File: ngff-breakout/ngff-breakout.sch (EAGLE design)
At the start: 79 parts, among them U1 MIC5366-1.8YC5, U2 MCP1827S-3302E/EB, X1 PINHD-2X4, X10 ZX360D-B-10P(30), X2 692121030100, X3 PINHD-2X10, X4 PINHD-2X5, X5 694108106102, X6 PINHD-1X3, X7 5-1814832-1, X8 5-1814832-1, X9 5-1814832-1, Y1 MHF4, Y2 MHF4, Y3 MHF4

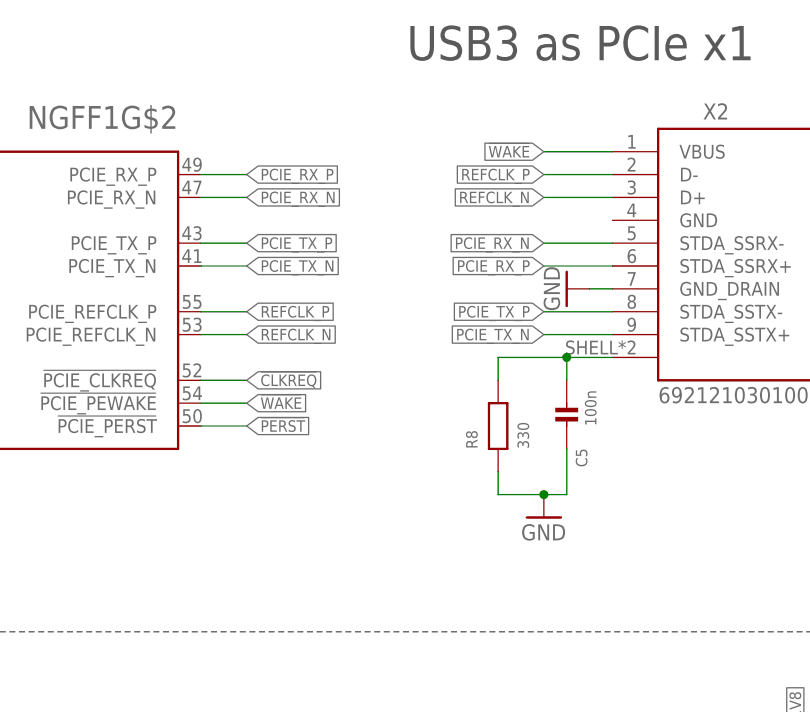
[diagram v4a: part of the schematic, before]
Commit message: ngff: swap Rx and Tx (solves OS#4230)
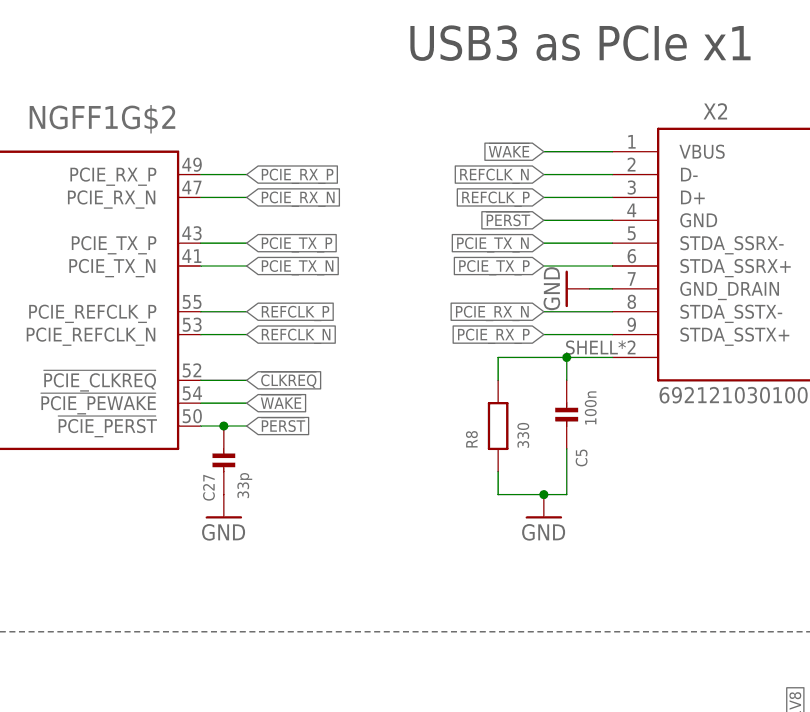
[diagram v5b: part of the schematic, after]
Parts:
- added C27: 33p, rc-sysmocom:CAP_CERAMIC_0402
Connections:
- net !PERST: now also C27.1, X2.GND
- net GND: now also C27.2
- net PCIE_RX_N: now also X2.STDA_SSTX-; no longer X2.STDA_SSRX-
- net PCIE_RX_P: now also X2.STDA_SSTX+; no longer X2.STDA_SSRX+
- net PCIE_TX_N: now also X2.STDA_SSRX-; no longer X2.STDA_SSTX+
- net PCIE_TX_P: now also X2.STDA_SSRX+; no longer X2.STDA_SSTX-
- net REFCLK_N: now also X2.D-; no longer X2.D+
- net REFCLK_P: now also X2.D+; no longer X2.D-
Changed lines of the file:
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@@
 </part>
 <part name="GND29" library="supply1" deviceset="GND" device=""/>
+<part name="C27" library="rc-sysmocom" deviceset="CAP_CERAMIC" device="_0402" value="33p">
+<attribute name="CLASS" value="CAPACITOR"/>
+<attribute name="DESCRIPTION" value="CAP CER 33PF 50V NP0 0402"/>
+<attribute name="LINK" value="http://www.digikey.de/product-detail/de/CL05C330JB5NNNC/1276-1272-1-ND/3889358"/>
+<attribute name="MANUFACTURER" value="Samsung Electro-Mechanics America, Inc."/>
+<attribute name="MANUFACTURERPARTNUMBER" value="CL05C330JB5NNNC"/>
+<attribute name="POPULATED" value="TRUE"/>
+<attribute name="ROHSCERTIFICATE" value="Bleifrei / RoHS-konform"/>
+<attribute name="SOURCE" value="DIGIKEY"/>
+<attribute name="SOURCEPARTNUMBER" value="1276-1272-1-ND"/>
+</part>
+<part name="GND36" library="supply1" deviceset="GND" device=""/>
 </parts>
 <sheets>
@@
 </instance>
 <instance part="GND29" gate="1" x="83.82" y="218.44" rot="R270"/>
+<instance part="C27" gate="G$1" x="45.72" y="200.66" smashed="yes" rot="R270">
+<attribute name="NAME" x="44.704" y="194.818" size="1.27" layer="95" rot="R90"/>
+<attribute name="VALUE" x="48.514" y="195.072" size="1.27" layer="96" rot="R90"/>
+<attribute name="DESCRIPTION" x="45.72" y="200.66" size="1.778" layer="96" display="off"/>
+<attribute name="MANUFACTURER" x="45.72" y="200.66" size="1.778" layer="96" display="off"/>
+<attribute name="MANUFACTURERPARTNUMBER" x="45.72" y="200.66" size="1.778" layer="96" display="off"/>
+<attribute name="SOURCE" x="45.72" y="200.66" size="1.778" layer="96" display="off"/>
+<attribute name="SOURCEPARTNUMBER" x="45.72" y="200.66" size="1.778" layer="96" display="off"/>
+<attribute name="ROHSCERTIFICATE" x="45.72" y="200.66" size="1.778" layer="96" display="off"/>
+<attribute name="POPULATED" x="45.72" y="200.66" size="1.778" layer="96" display="off"/>
+<attribute name="CLASS" x="45.72" y="200.66" size="1.778" layer="96" display="off"/>
+<attribute name="LINK" x="45.72" y="200.66" size="1.778" layer="96" display="off"/>
+</instance>
+<instance part="GND36" gate="1" x="45.72" y="193.04"/>
 </instances>
 <busses>
@@
 <pinref part="GND29" gate="1" pin="GND"/>
 <wire x1="86.36" y1="218.44" x2="88.9" y2="218.44" width="0.1524" layer="91"/>
+</segment>
+<segment>
+<pinref part="C27" gate="G$1" pin="2"/>
+<pinref part="GND36" gate="1" pin="GND"/>
 </segment>
 </net>
@@
 </segment>
 <segment>
+<label x="81.28" y="231.14" size="1.27" layer="95" rot="R180" xref="yes"/>
+<pinref part="X2" gate="G$1" pin="D-"/>
+<wire x1="81.28" y1="231.14" x2="88.9" y2="231.14" width="0.1524" layer="91"/>
+</segment>
+</net>
+<net name="REFCLK_P" class="1">
+<segment>
+<wire x1="43.18" y1="215.9" x2="48.26" y2="215.9" width="0.1524" layer="91"/>
+<label x="48.26" y="215.9" size="1.27" layer="95" rot="MR180" xref="yes"/>
+<pinref part="NGFF1" gate="G$2" pin="PCIE_REFCLK_P"/>
+</segment>
+<segment>
 <wire x1="88.9" y1="228.6" x2="81.28" y2="228.6" width="0.1524" layer="91"/>
 <label x="81.28" y="228.6" size="1.27" layer="95" rot="R180" xref="yes"/>
 <pinref part="X2" gate="G$1" pin="D+"/>
-</segment>
-</net>
-<net name="REFCLK_P" class="1">
-<segment>
-<wire x1="43.18" y1="215.9" x2="48.26" y2="215.9" width="0.1524" layer="91"/>
-<label x="48.26" y="215.9" size="1.27" layer="95" rot="MR180" xref="yes"/>
-<pinref part="NGFF1" gate="G$2" pin="PCIE_REFCLK_P"/>
-</segment>
-<segment>
-<wire x1="88.9" y1="231.14" x2="81.28" y2="231.14" width="0.1524" layer="91"/>
-<label x="81.28" y="231.14" size="1.27" layer="95" rot="R180" xref="yes"/>
-<pinref part="X2" gate="G$1" pin="D-"/>
 </segment>
 </net>
@@
 </segment>
 <segment>
+<label x="81.28" y="213.36" size="1.27" layer="95" rot="R180" xref="yes"/>
+<pinref part="X2" gate="G$1" pin="STDA_SSTX+"/>
+<wire x1="81.28" y1="213.36" x2="88.9" y2="213.36" width="0.1524" layer="91"/>
+</segment>
+</net>
+<net name="PCIE_RX_N" class="1">
+<segment>
+<pinref part="NGFF1" gate="G$2" pin="PCIE_RX_N"/>
+<wire x1="43.18" y1="228.6" x2="48.26" y2="228.6" width="0.1524" layer="91"/>
+<label x="48.26" y="228.6" size="1.27" layer="95" rot="MR180" xref="yes"/>
+</segment>
+<segment>
+<label x="81.28" y="215.9" size="1.27" layer="95" rot="R180" xref="yes"/>
+<pinref part="X2" gate="G$1" pin="STDA_SSTX-"/>
+<wire x1="81.28" y1="215.9" x2="88.9" y2="215.9" width="0.1524" layer="91"/>
+</segment>
+</net>
+<net name="PCIE_TX_P" class="1">
+<segment>
+<pinref part="NGFF1" gate="G$2" pin="PCIE_TX_P"/>
+<wire x1="43.18" y1="223.52" x2="48.26" y2="223.52" width="0.1524" layer="91"/>
+<label x="48.26" y="223.52" size="1.27" layer="95" rot="MR180" xref="yes"/>
+</segment>
+<segment>
 <label x="81.28" y="220.98" size="1.27" layer="95" rot="R180" xref="yes"/>
 <pinref part="X2" gate="G$1" pin="STDA_SSRX+"/>
@@
 </segment>
 </net>
-<net name="PCIE_RX_N" class="1">
-<segment>
-<pinref part="NGFF1" gate="G$2" pin="PCIE_RX_N"/>
-<wire x1="43.18" y1="228.6" x2="48.26" y2="228.6" width="0.1524" layer="91"/>
-<label x="48.26" y="228.6" size="1.27" layer="95" rot="MR180" xref="yes"/>
+<net name="PCIE_TX_N" class="1">
+<segment>
+<pinref part="NGFF1" gate="G$2" pin="PCIE_TX_N"/>
+<wire x1="43.18" y1="220.98" x2="48.26" y2="220.98" width="0.1524" layer="91"/>
+<label x="48.26" y="220.98" size="1.27" layer="95" rot="MR180" xref="yes"/>
 </segment>
 <segment>
@@
 <pinref part="X2" gate="G$1" pin="STDA_SSRX-"/>
 <wire x1="81.28" y1="223.52" x2="88.9" y2="223.52" width="0.1524" layer="91"/>
-</segment>
-</net>
-<net name="PCIE_TX_P" class="1">
-<segment>
-<pinref part="NGFF1" gate="G$2" pin="PCIE_TX_P"/>
-<wire x1="43.18" y1="223.52" x2="48.26" y2="223.52" width="0.1524" layer="91"/>
-<label x="48.26" y="223.52" size="1.27" layer="95" rot="MR180" xref="yes"/>
-</segment>
-<segment>
-<wire x1="88.9" y1="215.9" x2="81.28" y2="215.9" width="0.1524" layer="91"/>
-<label x="81.28" y="215.9" size="1.27" layer="95" rot="R180" xref="yes"/>
-<pinref part="X2" gate="G$1" pin="STDA_SSTX-"/>
-</segment>
-</net>
-<net name="PCIE_TX_N" class="1">
-<segment>
-<pinref part="NGFF1" gate="G$2" pin="PCIE_TX_N"/>
-<wire x1="43.18" y1="220.98" x2="48.26" y2="220.98" width="0.1524" layer="91"/>
-<label x="48.26" y="220.98" size="1.27" layer="95" rot="MR180" xref="yes"/>
-</segment>
-<segment>
-<wire x1="88.9" y1="213.36" x2="81.28" y2="213.36" width="0.1524" layer="91"/>
-<label x="81.28" y="213.36" size="1.27" layer="95" rot="R180" xref="yes"/>
-<pinref part="X2" gate="G$1" pin="STDA_SSTX+"/>
 </segment>
 </net>
@@
 <segment>
 <pinref part="NGFF1" gate="G$2" pin="!PCIE_PERST"/>
-<wire x1="43.18" y1="203.2" x2="48.26" y2="203.2" width="0.1524" layer="91"/>
+<wire x1="43.18" y1="203.2" x2="45.72" y2="203.2" width="0.1524" layer="91"/>
 <label x="48.26" y="203.2" size="1.27" layer="95" xref="yes"/>
+<pinref part="C27" gate="G$1" pin="1"/>
+<wire x1="45.72" y1="203.2" x2="48.26" y2="203.2" width="0.1524" layer="91"/>
+<junction x="45.72" y="203.2"/>
 </segment>
 <segment>
@@
 <pinref part="X3" gate="A" pin="10"/>
 </segment>
-</net>
+<segment>
+<pinref part="X2" gate="G$1" pin="GND"/>
+<wire x1="88.9" y1="226.06" x2="81.28" y2="226.06" width="0.1524" layer="91"/>
+<label x="81.28" y="226.06" size="1.27" layer="95" rot="R180" xref="yes"/>
+</segment>
+</net>

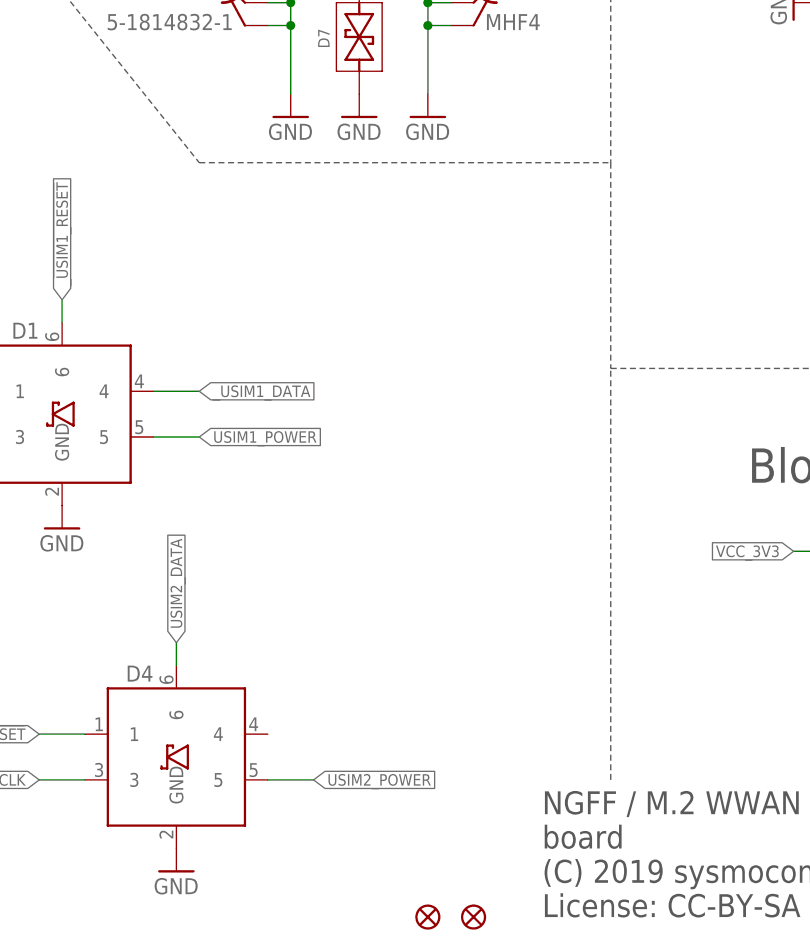
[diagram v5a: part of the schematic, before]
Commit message: ngff: PCB cosmetics and subsequent DRC; rearrange SMA + MHF4 conn
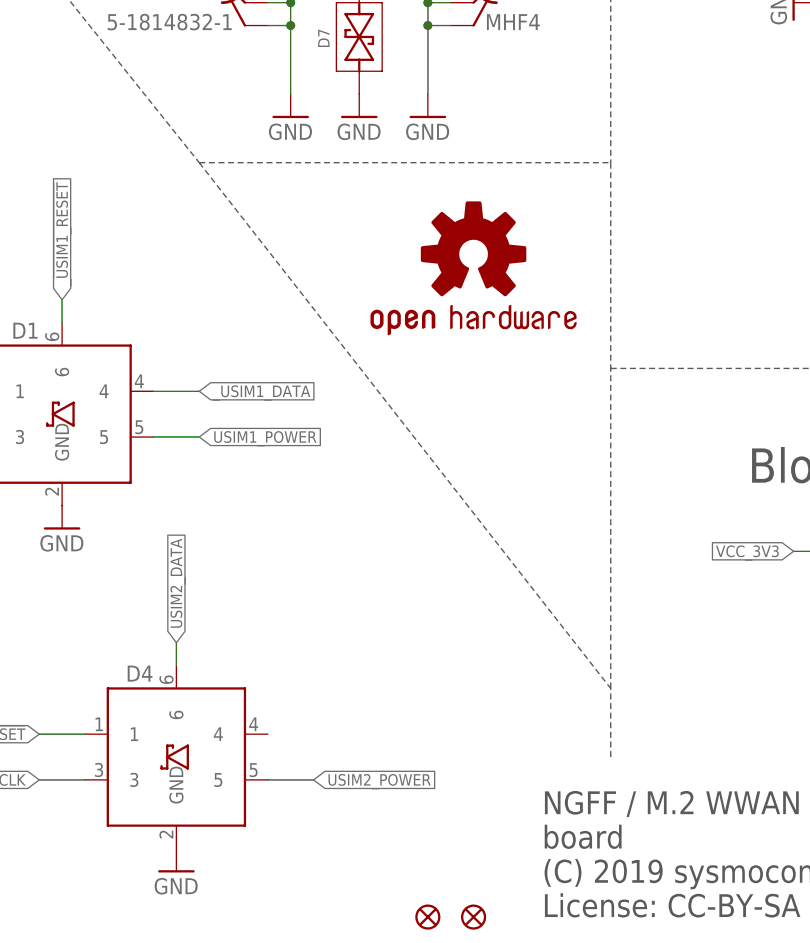
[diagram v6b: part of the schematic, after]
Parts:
- added LOGO1: OSHW-LOGOL-COPPER, SparkFun-Aesthetics:OSHW-LOGOL-COPPER
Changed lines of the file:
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@@
 <class number="3" name="supply" width="0.6" drill="0">
 <clearance class="0" value="0.3"/>
+<clearance class="3" value="0.3"/>
 </class>
 </classes>
@@
 </part>
 <part name="GND36" library="supply1" deviceset="GND" device=""/>
+<part name="LOGO1" library="SparkFun-Aesthetics" deviceset="OSHW-LOGO" device="L-COPPER"/>
 </parts>
 <sheets>
@@
 <wire x1="297.18" y1="68.58" x2="383.54" y2="68.58" width="0.1524" layer="97" style="longdash"/>
 <wire x1="251.46" y1="91.44" x2="297.18" y2="91.44" width="0.1524" layer="97" style="longdash"/>
-<wire x1="297.18" y1="22.86" x2="297.18" y2="68.58" width="0.1524" layer="97" style="longdash"/>
+<wire x1="297.18" y1="25.4" x2="297.18" y2="33.02" width="0.1524" layer="97" style="longdash"/>
+<wire x1="297.18" y1="33.02" x2="297.18" y2="68.58" width="0.1524" layer="97" style="longdash"/>
+<wire x1="251.46" y1="91.44" x2="297.18" y2="33.02" width="0.1524" layer="97" style="longdash"/>
 </plain>
 <instances>
@@
 </instance>
 <instance part="GND36" gate="1" x="45.72" y="193.04"/>
+<instance part="LOGO1" gate="G$1" x="281.94" y="81.28"/>
 </instances>
 <busses>
